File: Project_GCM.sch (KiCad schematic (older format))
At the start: 20 parts, among them J1 PowerSupply, J12 DEBUG_BUSES, J7 3-641124-6, U1 LM810, U11 74AHC1G04, U2 LTC6994xS6-1, U25 74AHC1G32, U3 74AHC1G32, U5 74AHC1G04

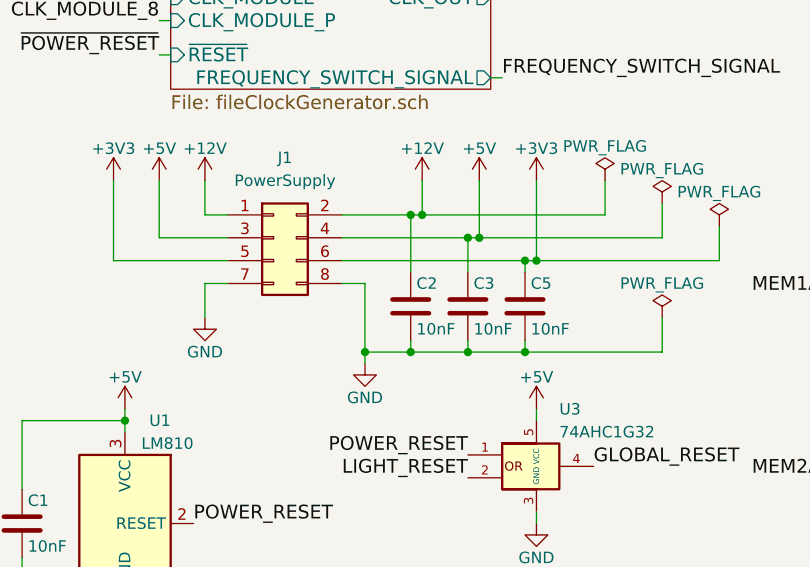
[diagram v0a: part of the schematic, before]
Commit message: Removed capacitor on 12V #11
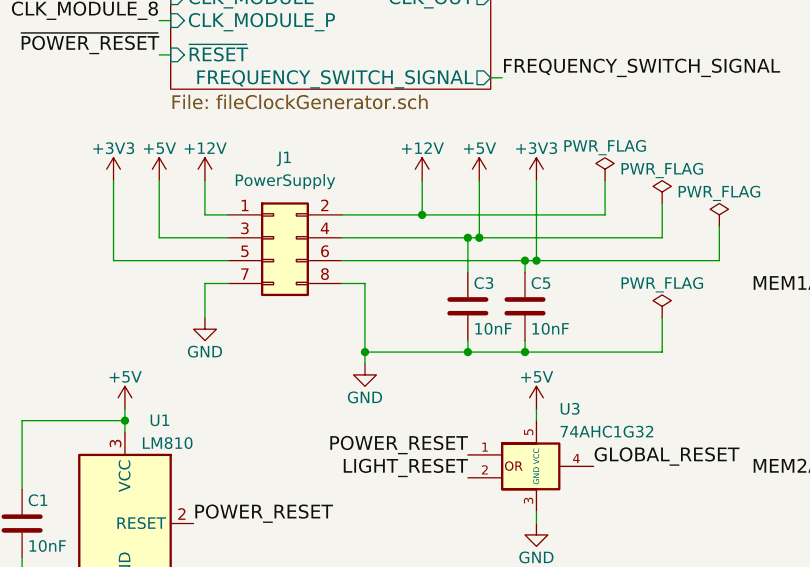
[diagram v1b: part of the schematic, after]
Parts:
- removed C2: 10nF, Capacitor_SMD:C_0805_2012Metric, symbol Device:C
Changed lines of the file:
@@
 $EndComp
-Wire Wire Line
-	2050 3700 2350 3700
 Wire Wire Line
 	1450 3550 1450 3700
@@
 	2150 4000 2050 4000
 $Comp
-L Device:C C2
-U 1 1 5B3D76C6
-P 2350 4100
-F 0 "C2" H 2375 4200 50  0000 L CNN
-F 1 "10nF" H 2375 4000 50  0000 L CNN
-F 2 "Capacitor_SMD:C_0805_2012Metric" H 2388 3950 50  0001 C CNN
-F 3 "" H 2350 4100 50  0001 C CNN
-	1    2350 4100
-	1    0    0    -1
-$EndComp
-$Comp
 L Device:C C3
 U 1 1 5B3E1786
@@
 Connection ~ 2600 3800
 Wire Wire Line
-	2350 3950 2350 3700
-Connection ~ 2350 3700
-Wire Wire Line
-	2150 4300 2350 4300
-Wire Wire Line
 	2850 4300 2850 4250
 Connection ~ 2150 4300
@@
 	2600 4300 2600 4250
 Connection ~ 2600 4300
-Wire Wire Line
-	2350 4300 2350 4250
-Connection ~ 2350 4300
 Text Label 3150 1350 0    60   ~ 0
 NUMBER_[0..7]
@@
 	2600 3800 2650 3800
 Wire Wire Line
-	2350 3700 2400 3700
-Wire Wire Line
 	2150 4300 2150 4350
 Wire Wire Line
 	2600 4300 2850 4300
-Wire Wire Line
-	2350 4300 2600 4300
 Wire Wire Line
 	2900 3900 3700 3900
@@
 Wire Wire Line
 	2400 3700 3200 3700
+Wire Wire Line
+	2050 3700 2400 3700
+Wire Wire Line
+	2150 4300 2600 4300
 Wire Bus Line
 	9000 1750 9000 2500

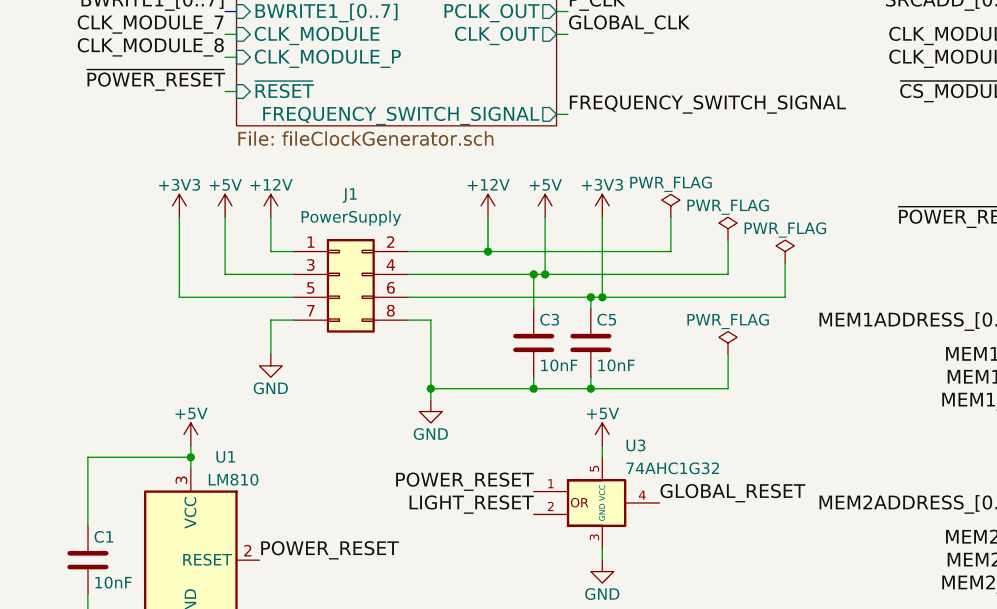
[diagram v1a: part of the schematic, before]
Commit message: Add/Modify power decoupling capacitor #10
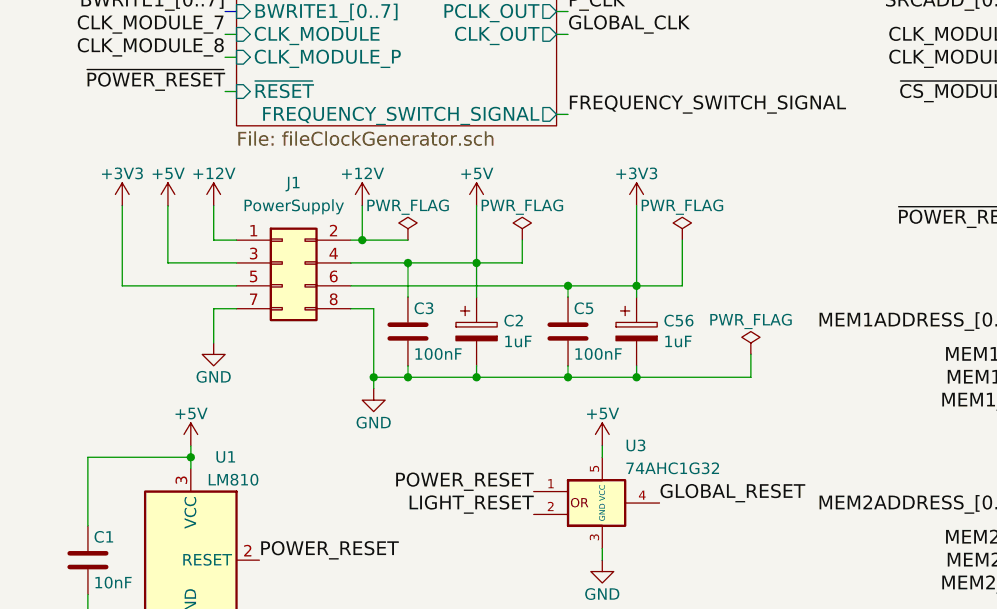
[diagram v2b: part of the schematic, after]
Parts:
- added C2, C56: 1uF, symbol Device:C_Polarized
- C3, C5: value 10nF -> 100nF
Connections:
- net +3V3: now also C56.1
- net +5V: now also C2.1
- net GND: now also C2.2, C56.2
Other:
- moved on the sheet: C3, C5, J1
